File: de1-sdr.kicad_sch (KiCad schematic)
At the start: 188 parts, among them J1 RF IN, J2 DE1-HEADER, J3 UFL, J4 UFL, J5 UFL, Q1 BSS138, Q2 AO3401A, T1 TC4-1TX+, U1 AD9609-80, U10 TPS7A2018DBV, U11 TPS7A2033DBV, U12 TPS7A2033DBV, U13 TPS7A2033DBV, U2 QPL9547, U3 MAX2682, U4 LMX2572, U5 BDA4620, U6 TPS7A2018DBV, U7 PAT1220-C-2DB, U8 BG18C, U9 BG18C, Y1 ECS-3518-800-B-TR

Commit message: todo: fix mixer matching, and LC footprints
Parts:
- C66: value 1.5n -> (none); now not fitted
- C69: value (none) -> 1.5n; now fitted
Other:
- moved on the sheet: C32

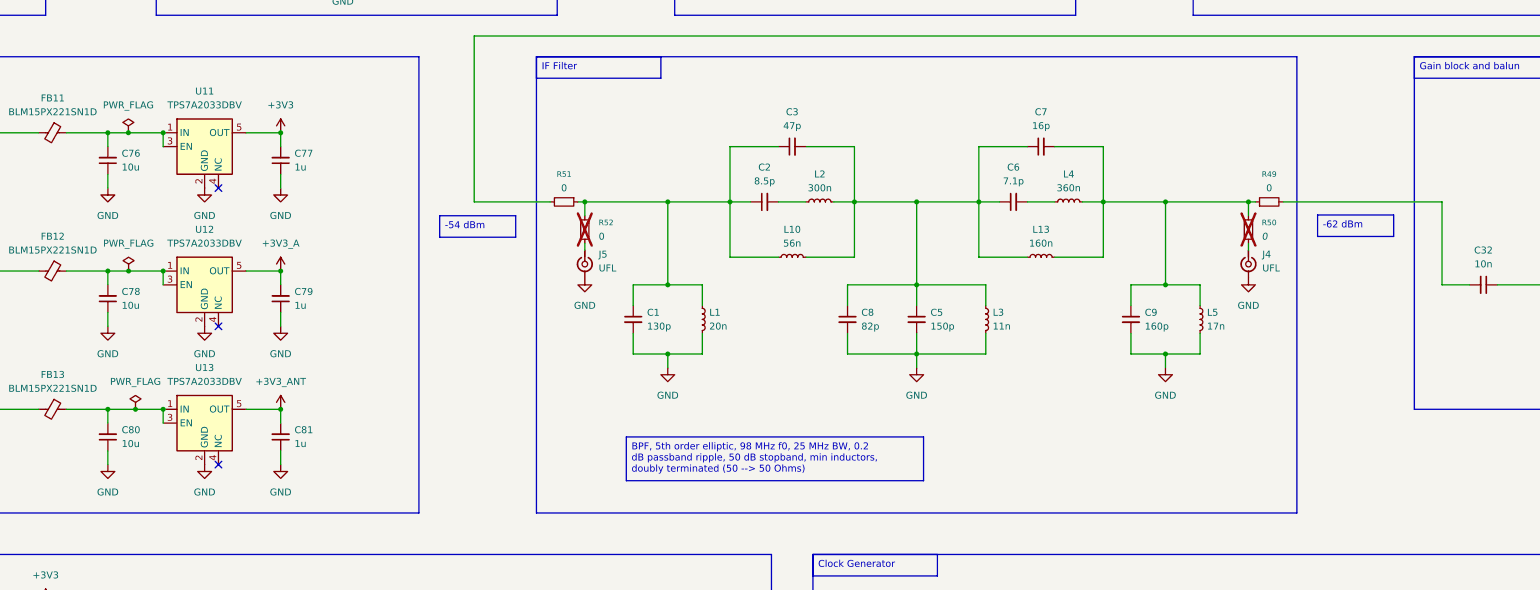
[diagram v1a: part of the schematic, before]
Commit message: fixed IF filter. todo: fix matching networks
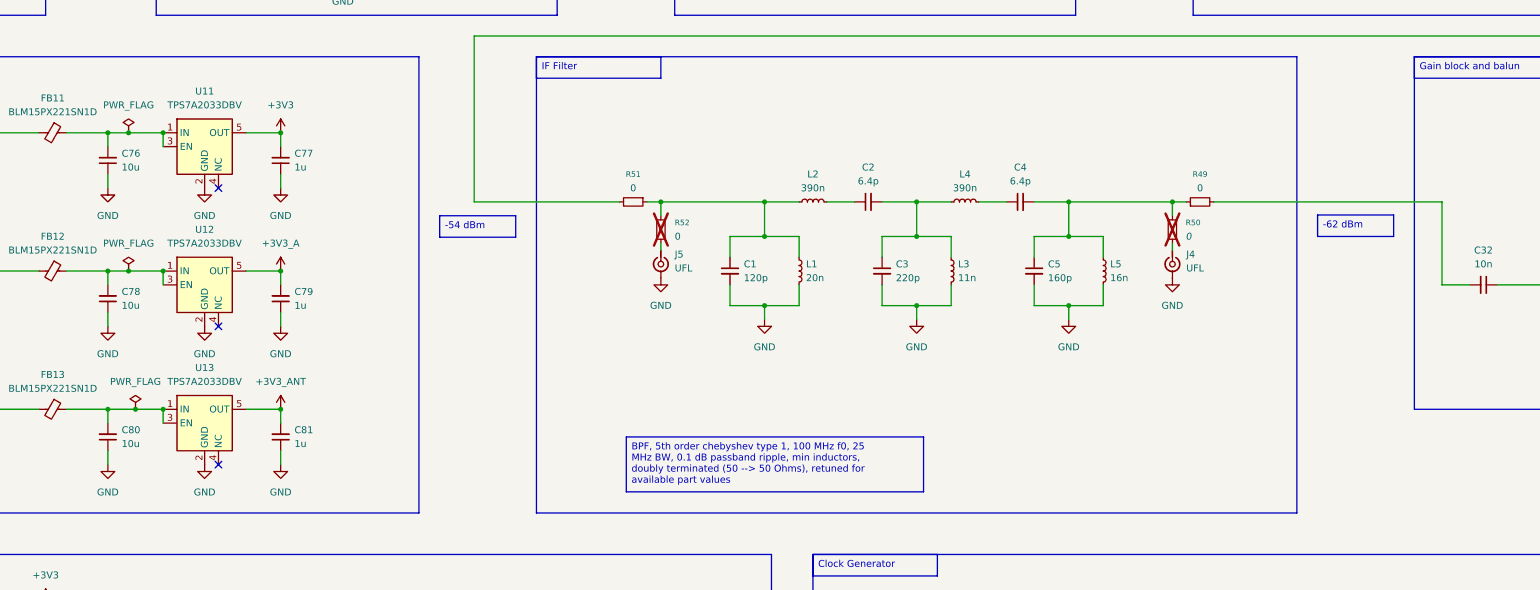
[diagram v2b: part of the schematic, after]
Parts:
- removed C6: 7.1p, Capacitor_SMD:C_0402_1005Metric, symbol Device:C_Small
- removed C7: 16p, Capacitor_SMD:C_0402_1005Metric, symbol Device:C_Small
- removed C8: 82p, Capacitor_SMD:C_0402_1005Metric, symbol Device:C_Small
- removed C9: 160p, Capacitor_SMD:C_0402_1005Metric, symbol Device:C_Small
- removed L10: 56n, Inductor_SMD:L_1008_2520Metric, symbol Device:L_Small
- removed L13: 160n, Inductor_SMD:L_0805_2012Metric, symbol Device:L_Small
- added C4: 6.4p, Capacitor_SMD:C_0402_1005Metric, symbol Device:C_Small
- C1: value 130p -> 120p
- C2: value 8.5p -> 6.4p
- C3: value 47p -> 220p
- C5: value 150p -> 160p; footprint Capacitor_SMD:C_0402_1005Metric -> Capacitor_SMD:C_0603_1608Metric
- J2: footprint (none) -> Connector_IDC:IDC-Header_2x20_P2.54mm_Vertical
- L1, L3: footprint Inductor_SMD:L_0805_2012Metric -> Inductor_SMD:L_0603_1608Metric
- L2: value 300n -> 390n; footprint Inductor_SMD:L_1008_2520Metric -> Inductor_SMD:L_0603_1608Metric
- L4: value 360n -> 390n; footprint Inductor_SMD:L_0805_2012Metric -> Inductor_SMD:L_0603_1608Metric
- L5: value 17n -> 16n; footprint Inductor_SMD:L_0603_1608Metric -> Capacitor_SMD:C_0603_1608Metric
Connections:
- net GND: now also C3.2
- net at L5.1, R49.1, R50.1: now also C5.1, C4.2; no longer L4.2
- net at C1.1, L1.1, R51.1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: now also L2.1; no longer C2.1, C3.1
- net at C2.2: now also C3.1, L3.1, L4.1; no longer L2.1
- new net: C2.1, L2.2
- new net: C4.1, L4.2
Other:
- moved on the sheet: C1, J4, J5, L1, R49, R50, R51, R52

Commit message: start placement
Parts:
- removed C18: 100p, Capacitor_SMD:C_0402_1005Metric, symbol Device:C_Small
- removed R14: 1k, Resistor_SMD:R_0402_1005Metric, symbol Device:R_Small
- added C6: 27p, Capacitor_SMD:C_0402_1005Metric, symbol Device:C_Small
- added C7: 130p, Capacitor_SMD:C_0402_1005Metric, symbol Device:C_Small
- added C8: 10u, Capacitor_SMD:C_0603_1608Metric, symbol Device:C_Small
- added C86: 100p, Capacitor_SMD:C_0402_1005Metric, symbol Device:C_Small
- added C9: 1u, Capacitor_SMD:C_0402_1005Metric, symbol Device:C_Small
- added D1: ESD601DPYRQ1, Diode_SMD:D_0402_1005Metric, symbol Device:D_TVS
- added D2, D3, D4: LED, LED_SMD:LED_0603_1608Metric, symbol Device:LED
- added L10: 330n, Inductor_SMD:L_1008_2520Metric, symbol Device:L_Small
- added L13: 62n, Inductor_SMD:L_0603_1608Metric, symbol Device:L_Small
- added R1: 1k, Resistor_SMD:R_0201_0603Metric, symbol Device:R_Small
- added R53, R54: 0, Resistor_SMD:R_0402_1005Metric, symbol Device:R_Small
- added R55: (no value), Resistor_SMD:R_0402_1005Metric, symbol Device:R_Small
- added R56, R57, R58: 1k, Resistor_SMD:R_0402_1005Metric, symbol Device:R_Small
- C1: value 120p -> 91p
- C2: value 6.4p -> 62p
- C23: value 270p -> (none)
- C24: value 15p -> (none)
- C3: value 220p -> 36p
- C34: value DNI -> 10p; now fitted
- C4: value 6.4p -> 180p
- C5: value 160p -> 22p; footprint Capacitor_SMD:C_0603_1608Metric -> Capacitor_SMD:C_0402_1005Metric
- L1: value 20n -> 82n; footprint Inductor_SMD:L_0603_1608Metric -> Inductor_SMD:L_0805_2012Metric
- L11, L12: value 1u -> 2.7u; footprint Inductor_SMD:L_1008_2520Metric -> Inductor_SMD:L_1210_3225Metric
- L2: value 390n -> 220n; footprint Inductor_SMD:L_0603_1608Metric -> Inductor_SMD:L_0805_2012Metric
- L3: value 11n -> 130n; footprint Inductor_SMD:L_0603_1608Metric -> Inductor_SMD:L_0805_2012Metric
- L4: value 390n -> 43n
- L5: value 16n -> 300n; footprint Capacitor_SMD:C_0603_1608Metric -> Inductor_SMD:L_0805_2012Metric
- L6: footprint Inductor_SMD:L_1812_4532Metric_Pad1.30x3.40mm_HandSolder -> 0thaumati-footprintslib:AC5037SQ-68NJ
- L8: value 2.2n -> (none)
- L9: value 330n -> (none); footprint Inductor_SMD:L_0402_1005Metric -> Inductor_SMD:L_0805_2012Metric
- R10, R11, R12, R13, R20, R21, R22, R23, R24, R25, R26, R27, R28, R29, R30, R31, R32, R5, R6, R7, R8, R9: footprint Resistor_SMD:R_0402_1005Metric -> Resistor_SMD:R_0201_0603Metric
- R16, R17: value 100 -> 33
- R46: value 1k -> 1.2k
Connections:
- net +3V3: now also D2.2 (A), R1.2
- net +3V3_A: now also C8.2; no longer C21.2
- net +5V_IN: now also D4.2 (A)
- net ADC_INM: now also C34.1, R16.1; no longer C34.2, R17.1
- net ADC_INP: now also C34.2, R17.1; no longer C34.1, R16.1
- net DSA_D0: now also R8.2; no longer R5.2
- net DSA_D1: now also R9.2; no longer R6.2
- net DSA_D2: now also R10.2; no longer R7.2
- net DSA_D3: now also R11.2; no longer R8.2
- net DSA_D4: now also R12.2; no longer R9.2
- net DSA_D5: now also R13.2; no longer R10.2
- net GND: now also C23.1, C4.2, L4.2, R5.2, R6.2, R7.2, C7.2, C8.1, C9.1, D1.1 (A1), L13.2, R55.1, R56.2, R57.2, R58.2; no longer C3.2, C5.2, L3.2, L5.2, L8.2, R11.2, R12.2, R13.2
- net at U5.1 (D5): now also R13.1; no longer R10.1
- net at U5.13 (P/S): now also R7.1; no longer R11.1
- net at U5.15 (D4): now also R12.1; no longer R9.1
- net at U5.16 (D3): now also R11.1; no longer R8.1
- net at U5.17 (D2): now also R10.1; no longer R7.1
- net at U5.19 (D1): now also R9.1; no longer R6.1
- net at U5.20 (D0): now also R8.1; no longer R5.1
- net at U5.3 (SERIN): now also R6.1; no longer R12.1
- net at U5.4 (CLK): now also R5.1; no longer R13.1
- net at U5.5 (LE): now also R1.1
- net at C19.2, L6.1, Q2.3 (D): now also C21.2, C9.2
- net at C10.1, J1.1 (In), L6.2: now also D1.2 (A2)
- net at C2.1: now also C1.1, L1.1, L2.1, L3.1, R51.1, R52.1; no longer L2.2
- net at C2.2, L4.1: now also C3.2, C4.1, C5.1, L3.2, L5.1, L10.1; no longer C3.1, L3.1
- net at C23.2: now also L8.1, R54.2; no longer U3.3 (RFIN)
- net LED1: now reaches J2.4 (Pin_4)
- net LED1: now also D3.2 (A)
- net at C24.1, L9.2: now also R53.2; no longer U3.4 (IFOUT)
- new net: D3.1 (K), R57.1
- new net: C6.1, L5.2
- new net: C5.2, C6.2, C7.1, L10.2, L13.1, R49.1, R50.1
- new net: C86.2, U5.14 (RF2)
- new net: D2.1 (K), R56.1
- new net: L8.2, R55.2, U3.3 (RFIN)
- new net: R53.1, U3.4 (IFOUT)
- new net: C86.1, R54.1
- new net: C3.1, L2.2
- new net: D4.1 (K), R58.1
- no-connect marks 19 -> 18
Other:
- moved on the sheet: C19, C23, C29, C30, C31, C32, C33, C49, FB1, J1, J4, J5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

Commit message: routed pcb
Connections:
- net +5V_IN: now also J2.29 (Pin_29); no longer J2.11 (Pin_11)
- net ADC_DCO: now also J2.39 (Pin_39); no longer J2.1 (Pin_1)
- net ADC_MODE_OR: now also J2.35 (Pin_35); no longer J2.5 (Pin_5)
- net ADC_SPI_CS: now also J2.33 (Pin_33); no longer J2.7 (Pin_7)
- net ADC_SPI_SCLK: now also J2.31 (Pin_31); no longer J2.9 (Pin_9)
- net ADC_SPI_SDIO: now also J2.27 (Pin_27); no longer J2.13 (Pin_13)
- net ANT_PWR_EN: now also J2.2 (Pin_2); no longer J2.40 (Pin_40)
- net DSA_D0: now also J2.15 (Pin_15); no longer J2.25 (Pin_25)
- net DSA_D1: now also J2.13 (Pin_13); no longer J2.27 (Pin_27)
- net DSA_D2: now also J2.9 (Pin_9); no longer J2.31 (Pin_31)
- net DSA_D3: now also J2.7 (Pin_7); no longer J2.33 (Pin_33)
- net DSA_D4: now also J2.5 (Pin_5); no longer J2.35 (Pin_35)
- net DSA_D5: now also J2.3 (Pin_3); no longer J2.37 (Pin_37)
- net LED1: now also J2.38 (Pin_38); no longer J2.4 (Pin_4)
- net LNA_EN: now also J2.1 (Pin_1); no longer J2.39 (Pin_39)
- net MIXER_SHDN: now also J2.40 (Pin_40); no longer J2.2 (Pin_2)
- net PLL_EN: now also J2.23 (Pin_23); no longer J2.17 (Pin_17)
- net PLL_MUXOUT: now also J2.25 (Pin_25); no longer J2.15 (Pin_15)
- net PLL_SPI_CS: now also J2.17 (Pin_17); no longer J2.23 (Pin_23)
- net PLL_SPI_MOSI: now also J2.19 (Pin_19); no longer J2.21 (Pin_21)
- net PLL_SPI_SCLK: now also J2.21 (Pin_21); no longer J2.19 (Pin_19)
- net XO_EN: now also J2.4 (Pin_4); no longer J2.38 (Pin_38)
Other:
- moved on the sheet: J3
